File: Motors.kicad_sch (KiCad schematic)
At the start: 0 parts

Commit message: filled in the four MOSFETS for motor control
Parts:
- added D1, D2, D3, D4: SS14, Diode_SMD:D_SMA, symbol Diode:SS14
- added J1, J2, J3, J4: Conn_01x02_Pin, Connector_AMASS:AMASS_XT30PW-F_1x02_P2.50mm_Horizontal, symbol Connector:Conn_01x02_Pin
- added Q1, Q2, Q3, Q4: AO3400A, Package_TO_SOT_SMD:SOT-23, symbol Transistor_FET:AO3400A
- added R1, R3, R5, R7: 47R, symbol Device:R
- added R2, R4, R6, R8: 10k, symbol Device:R
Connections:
- new net: Q1.1 (G), R1.2, R2.1
- new net: D1.2 (A), J1.1 (Pin_1), Q1.3 (D)
- new net: Q2.1 (G), R3.2, R4.1
- new net: Q4.1 (G), R7.2, R8.1
- new net: D2.2 (A), J2.1 (Pin_1), Q2.3 (D)
- new net: D3.2 (A), J3.1 (Pin_1), Q3.3 (D)
- new net: Q3.1 (G), R5.2, R6.1
- new net: D4.2 (A), J4.1 (Pin_1), Q4.3 (D)
- new net +BATT: D1.1 (K), D2.1 (K), D3.1 (K), D4.1 (K), J1.2 (Pin_2), J2.2 (Pin_2), J3.2 (Pin_2), J4.2 (Pin_2)
- new net GND: Q1.2 (S), Q2.2 (S), Q3.2 (S), Q4.2 (S), R2.2, R4.2, R6.2, R8.2
- new net MOTOR 1: R1.1
- new net MOTOR 2: R3.1
- new net MOTOR 3: R5.1
- new net MOTOR 4: R7.1
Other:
- note added: "Flyback diode To block the current when on When motor off, it lets the motor's flyback current go through itself again and not the MOSFET."
- note added: "Notes: N channel mosfet, will allow top to flow to bottom when gate is driven high"
- note added: "Notes: We call this +BATT and not 3.3V because this will be pulled from the battery and the voltage regulator."
- note added: "Pull Down Resistor"
- note added: "Series resistor to limit impulse current"
- title: (none) -> Motor Schematic

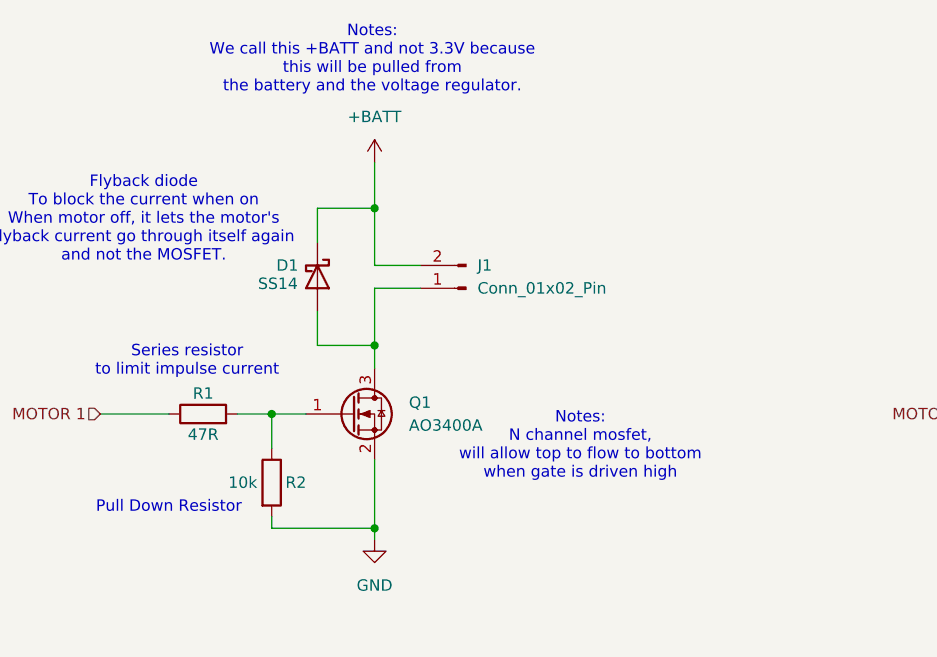
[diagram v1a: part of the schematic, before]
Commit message: Finished motor and battery/regulator subfolders
Also made a folder for holding datasheets.
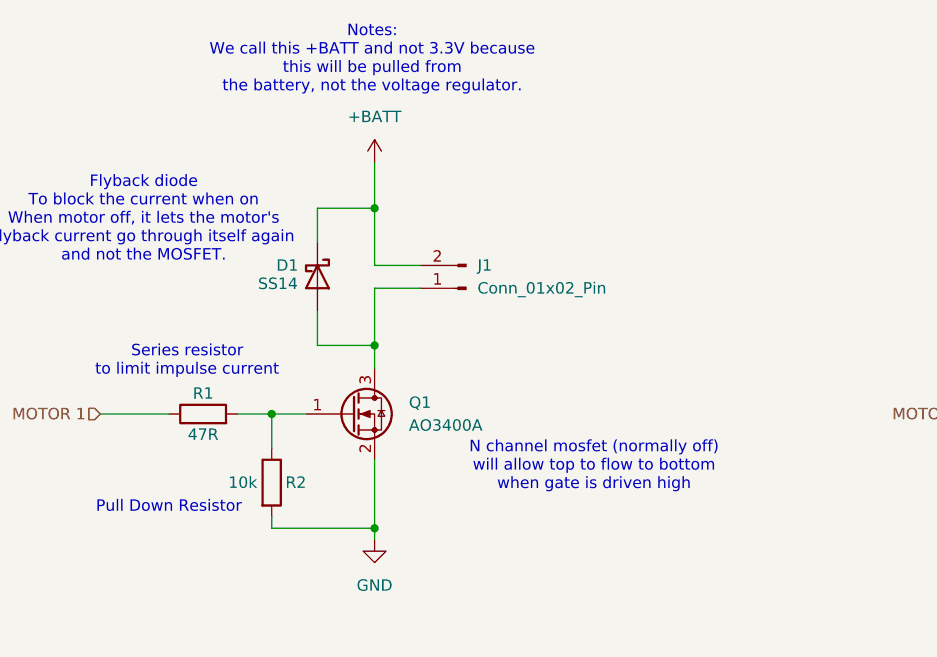
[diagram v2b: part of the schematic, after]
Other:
- note added: "N channel mosfet (normally off) will allow top to flow to bottom when gate is driven high"
- note added: "Notes: We call this +BATT and not 3.3V because this will be pulled from the battery, not the voltage regulator."
- note removed: "Notes: N channel mosfet, will allow top to flow to bottom when gate is driven high"
- note removed: "Notes: We call this +BATT and not 3.3V because this will be pulled from the battery and the voltage regulator."
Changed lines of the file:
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@@
 		)
 	)
-	(text "Notes:\nWe call this +BATT and not 3.3V because \nthis will be pulled from \nthe battery and the voltage regulator."
+	(text "Notes:\nWe call this +BATT and not 3.3V because \nthis will be pulled from \nthe battery, not the voltage regulator."
 		(exclude_from_sim no)
 		(at 114.046 34.29 0)
@@
 		)
 	)
-	(text "Notes:\nN channel mosfet, \nwill allow top to flow to bottom \nwhen gate is driven high"
+	(text "N channel mosfet (normally off)\nwill allow top to flow to bottom \nwhen gate is driven high"
 		(exclude_from_sim no)
-		(at 137.16 77.216 0)
+		(at 138.684 79.502 0)
 		(effects
 			(font
